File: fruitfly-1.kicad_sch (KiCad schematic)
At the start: 0 parts

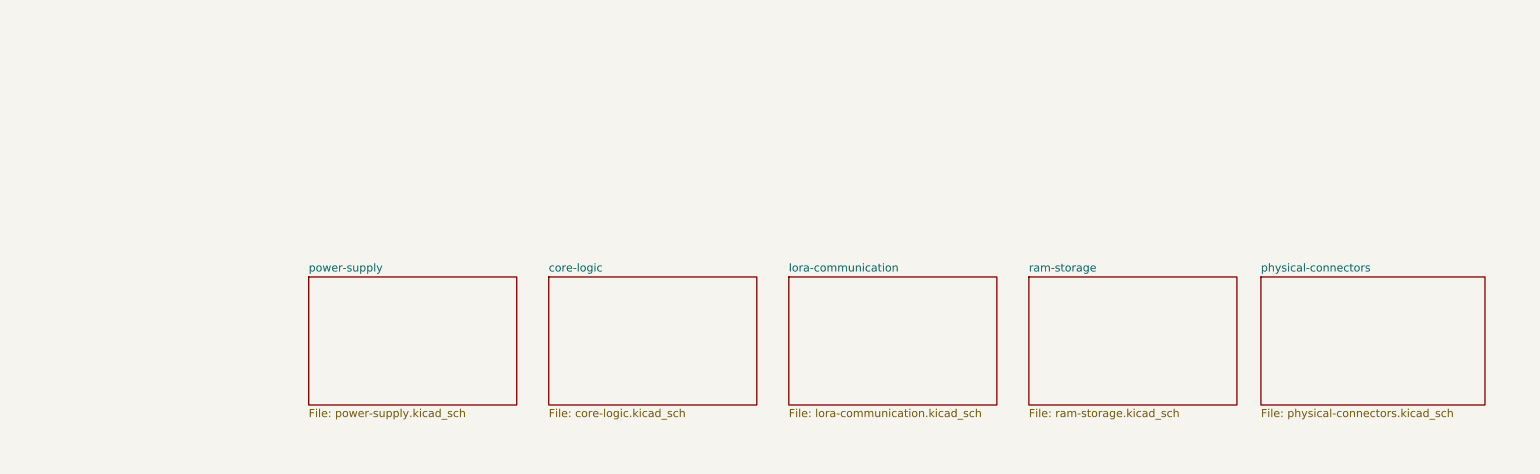
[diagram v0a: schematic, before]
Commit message: updated bus aliases; added resistor values to RF section; added component to Fruitly_RF library
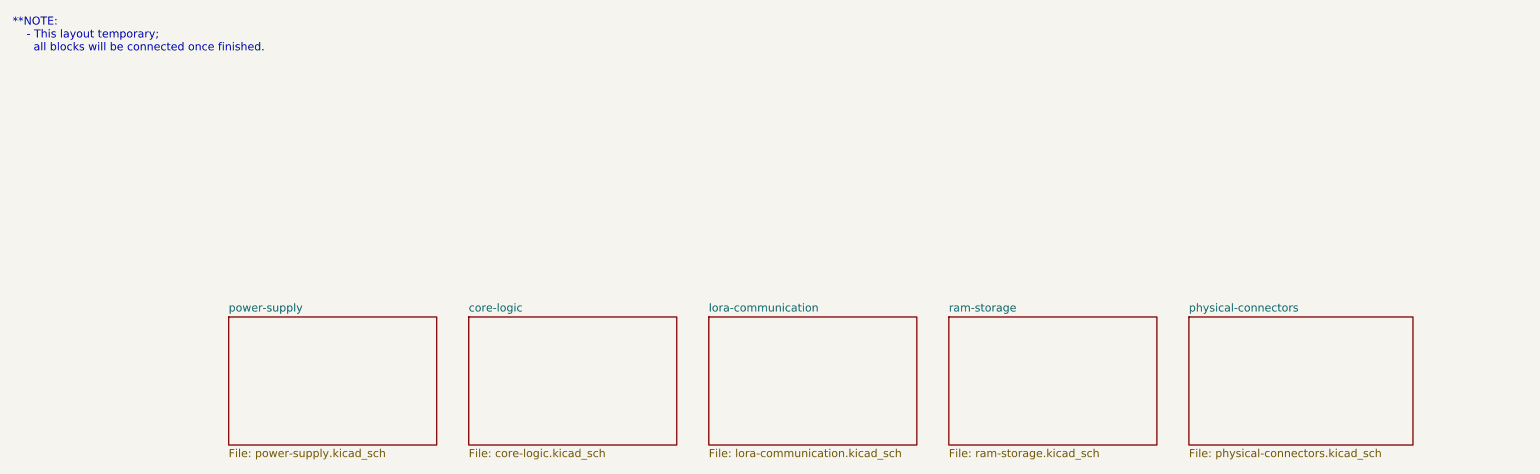
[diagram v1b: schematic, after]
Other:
- note added: "**NOTE: - This layout temporary; all blocks will be connected once finished."
- company: (none) -> Cerebral Systems Inc.
- title: (none) -> Fruitfly Node
